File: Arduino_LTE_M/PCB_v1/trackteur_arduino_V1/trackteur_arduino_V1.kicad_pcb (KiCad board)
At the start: 2 copper layers, 94.7 x 56.3 mm, 24 parts, among them J1 rPi_HDR, J2 DC/DC, J3 BATT_CAR, J4 MicroSD_Breakout, Q1 2N3904, U1 LD1117S33TR_SOT223

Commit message: update PCB
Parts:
- removed H6, H7: MountingHole_2.7mm_M2.5, MountingHole:MountingHole_2.7mm_M2.5
- added G***: LOGO, footprint_project:logo_trackteur, B.Cu at (208.0, 83.7)
- added H2: MountingHole, MountingHole:MountingHole_2.7mm_M2.5, F.Cu at (134.1, 65.9)
- added H3: MountingHole, MountingHole:MountingHole_2.7mm_M2.5, F.Cu at (134.1, 72.9)
- added J5: Conn_02x02_Counter_Clockwise, Connector_PinHeader_2.54mm:PinHeader_2x02_P2.54mm_Vertical, F.Cu at (243.2, 50.0)
- added J6: Conn_01x06, Connector_PinHeader_2.54mm:PinHeader_1x06_P2.54mm_Vertical, F.Cu at (218.9, 69.8)
- added TP1: +5V, Connector_PinHeader_2.54mm:PinHeader_1x01_P2.54mm_Vertical, F.Cu at (167.0, 90.5)
- added TP2: GND, Connector_PinHeader_2.54mm:PinHeader_1x01_P2.54mm_Vertical, F.Cu at (176.1, 90.6)
- added TP3: +3.3V, Connector_PinHeader_2.54mm:PinHeader_1x01_P2.54mm_Vertical, F.Cu at (180.8, 74.8)
- H1: value MountingHole_2.7mm_M2.5 -> MountingHole
- moved Q1 34.0 mm to (167.3, 77.9), turned to -90 degrees
- moved R1 33.8 mm to (171.9, 84.0), turned to 90 degrees
- moved R2 30.6 mm to (162.3, 79.0)
- moved R4 30.0 mm to (186.8, 52.2), turned to -90 degrees
- moved H1 27.5 mm to (134.1, 59.0)
- moved D4 24.0 mm to (191.1, 62.5), turned to 90 degrees
- moved R3 14.1 mm to (201.6, 71.1), turned to 180 degrees
- moved C1 10.1 mm to (186.3, 93.1)
- moved D2 9.83 mm to (234.1, 74.3)
- moved D3 2.65 mm to (214.5, 71.0)
- moved D1 2.44 mm to (236.3, 93.9)
- moved C2 2.16 mm to (180.3, 84.6), turned to 90 degrees
- moved J3 0.45 mm to (243.8, 86.8)
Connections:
- A1 pad 10: unconnected-(A1-D7-Pad10) -> D7
- A1 pad 13: unconnected-(A1-D10-Pad13) -> D10
- A1 pad 19: unconnected-(A1-A0-Pad19) -> A0
- A1 pad 20: unconnected-(A1-A1-Pad20) -> A1
- A1 pad 21: unconnected-(A1-A2-Pad21) -> A2
- A1 pad 22: unconnected-(A1-A3-Pad22) -> A3
- A1 pad 8: unconnected-(A1-D5-Pad8) -> D5
- A1 pad 9: unconnected-(A1-D6-Pad9) -> D9
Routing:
- net GND: track 0.00 -> 228.5 mm
- net +5V: track 0.00 -> 171.4 mm
- net SCK: track 0.00 -> 70.3 mm, vias 0 -> 1
- net DI: track 0.00 -> 68.8 mm, vias 0 -> 1
- net TXD: track 0.00 -> 68.5 mm
- net DO: track 0.00 -> 68.0 mm, vias 0 -> 1
- net RXD: track 0.00 -> 66.2 mm
- net /CS: track 0.00 -> 60.9 mm
- net CD: track 0.00 -> 55.3 mm, vias 0 -> 1
- net TXD_5V: track 0.00 -> 52.0 mm
- net +3.3V: track 0.00 -> 44.5 mm
- net Net-(D2-A1): track 0.00 -> 25.6 mm
- net CTL: track 0.00 -> 20.0 mm
- net CTL_5V: track 0.00 -> 19.5 mm
- net Net-(D1-A): track 0.00 -> 14.8 mm
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
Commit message: Fichiers de fabrication
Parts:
- added G***: LOGO, footprint_project:logo_trackteur, F.Cu at (172.3, 48.4)
- J3: footprint Connector_Wire:SolderWire-0.75sqmm_1x02_P7mm_D1.25mm_OD3.5mm -> Connector_Wire:SolderWire-2.5sqmm_1x02_P7.2mm_D2.4mm_OD3.6mm
- moved H2 114.0 mm to (244.9, 92.8)
- moved H3 31.2 mm to (158.1, 92.8)
- moved H1 28.0 mm to (158.1, 44.6)
- moved G*** 7.78 mm to (200.5, 81.5)
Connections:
- J5 pad 1: A3 -> A2
- J5 pad 2: A2 -> A3
- J5 pad 3: A1 -> A0
- J5 pad 4: A0 -> A1
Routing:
- net GND: track 228.5 -> 271.4 mm
- net +5V: track 171.4 -> 208.0 mm
- net A3: track 0.00 -> 29.4 mm
- net A1: track 0.00 -> 24.8 mm
- net A2: track 0.00 -> 23.4 mm
- net A0: track 0.00 -> 18.1 mm
- net D5: track 0.00 -> 8.07 mm
- net D9: track 0.00 -> 7.12 mm
- net D7: track 0.00 -> 7.12 mm
- net D10: track 0.00 -> 4.00 mm
- net CTL: track 20.0 -> 19.5 mm
- added copper zone on B.Cu, net GND
- added copper zone on F.Cu, net GND
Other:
- board size 94.7 x 56.3 mm -> 95.4 x 56.8 mm
- board text added: "+5V"
- board text added: "/CS"
- board text added: "A0"
- board text added: "A1"
- board text added: "A2"
- board text added: "A3"
- board text added: "CD"
- board text added: "D10"
- board text added: "D5"
- board text added: "D7"
- board text added: "D9"
- board text added: "DI"
- board text added: "DO"
- board text added: "GND"
- board text added: "M2.5"
- board text added: "SCK"
- board text added: "v2025.04.01"

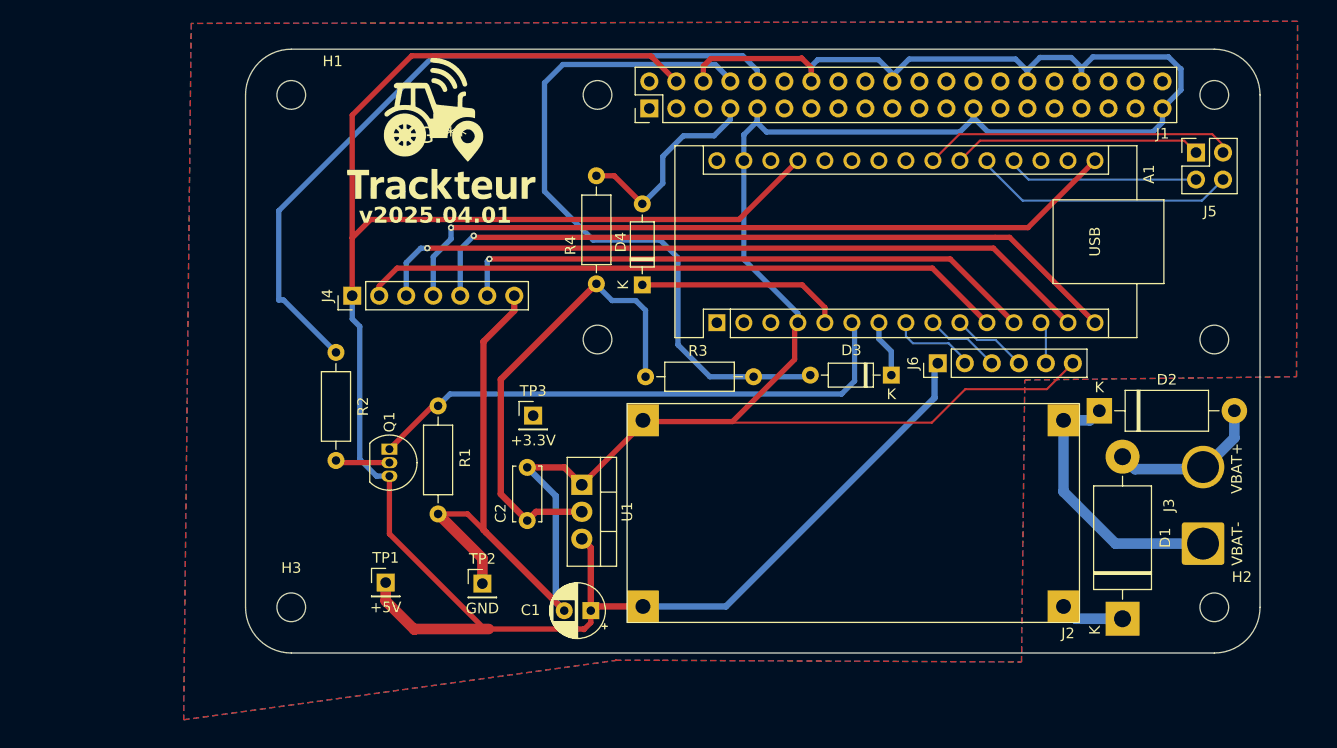
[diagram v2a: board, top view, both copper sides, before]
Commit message: LTE send dummy gps working and new pcb
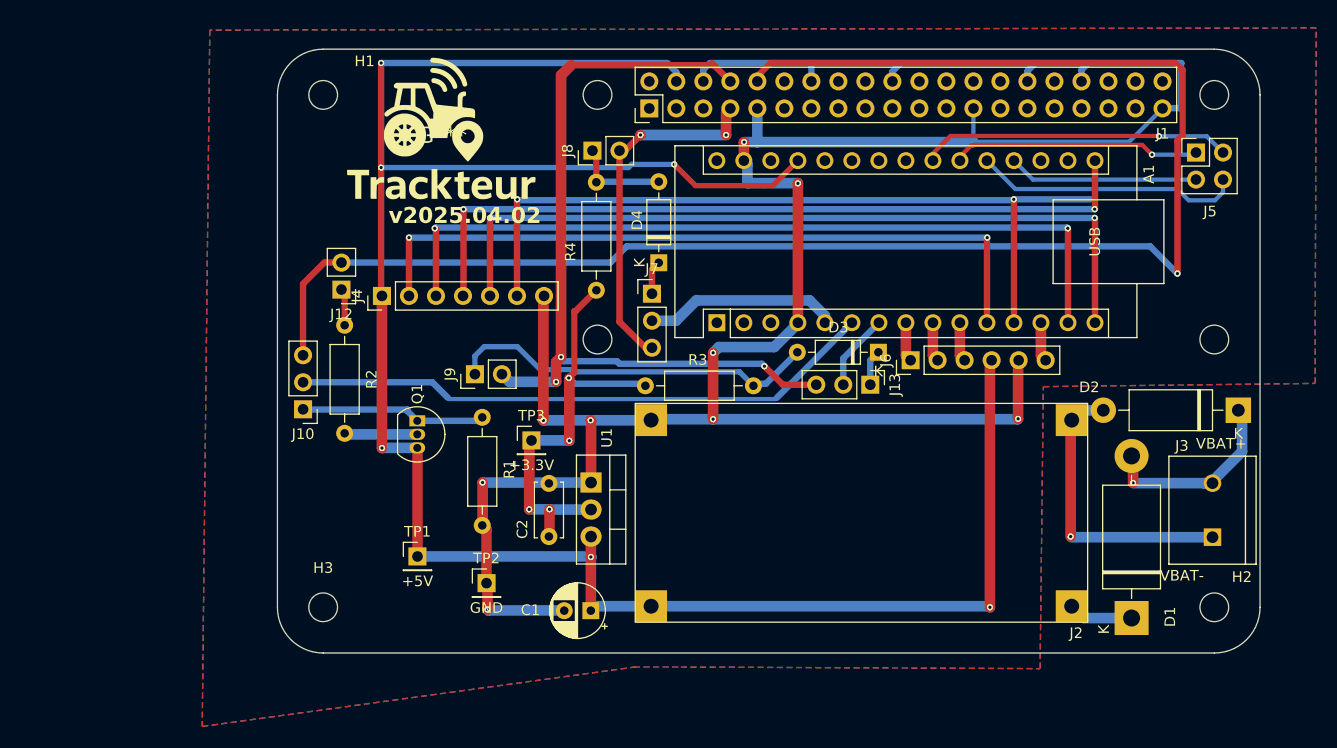
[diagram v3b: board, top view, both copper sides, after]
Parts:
- added J10: Conn_01x03, Connector_PinHeader_2.54mm:PinHeader_1x03_P2.54mm_Vertical, F.Cu at (159.2, 74.2)
- added J12: Conn_01x02, Connector_PinHeader_2.54mm:PinHeader_1x02_P2.54mm_Vertical, F.Cu at (162.8, 62.9)
- added J13: Conn_01x03, Connector_PinHeader_2.54mm:PinHeader_1x03_P2.54mm_Vertical, F.Cu at (212.6, 71.9)
- added J7: Conn_01x03, Connector_PinHeader_2.54mm:PinHeader_1x03_P2.54mm_Vertical, F.Cu at (192.0, 63.3)
- added J8: Conn_01x02, Connector_PinHeader_2.54mm:PinHeader_1x02_P2.54mm_Vertical, F.Cu at (186.4, 49.9)
- added J9: Conn_01x02, Connector_PinHeader_2.54mm:PinHeader_1x02_P2.54mm_Vertical, F.Cu at (175.4, 70.9)
- J3: footprint Connector_Wire:SolderWire-2.5sqmm_1x02_P7.2mm_D2.4mm_OD3.6mm -> footprint_project:TE_282837-2
- moved D2 13.1 mm to (247.2, 74.3), turned to 180 degrees
- moved R1 4.29 mm to (176.1, 85.1)
- moved TP1 3.87 mm to (170.0, 88.0)
- moved Q1 3.73 mm to (169.9, 75.3)
- moved J3 3.27 mm to (244.7, 83.7)
- moved H1 3.00 mm to (161.1, 44.6)
- moved H3 3.00 mm to (161.1, 92.8)
- moved J4 2.80 mm to (166.6, 63.5)
- moved R2 2.68 mm to (163.1, 76.4)
- moved D4 2.60 mm to (192.7, 60.4)
- moved J6 2.57 mm to (216.3, 69.6)
- moved C2 2.54 mm to (182.3, 86.2)
- moved D3 2.47 mm to (213.3, 68.8)
- moved TP3 2.34 mm to (180.7, 77.1)
- moved U1 0.89 mm to (186.3, 81.1)
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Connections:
- net Net-(D1-K) renamed /VBAT+2
- D1 pad 2: Net-(D1-A) -> /VBAT+
- D2 pad 1: Net-(D2-A1) -> /VBAT+
- D2 pad 2: Net-(D1-A) -> /VBAT-
- D3 pad 1: RXD_5V -> Net-(D3-K)
- D3 pad 2: RXD -> Net-(D3-A)
- D4 pad 1: CTL_5V -> Net-(D4-K)
- D4 pad 2: CTL -> Net-(D4-A)
- J2 pad 3: Net-(D2-A1) -> /VBAT-
- J3 pad 1: Net-(D2-A1) -> /VBAT-
- J3 pad 2: Net-(D1-A) -> /VBAT+
- J6 pad 1: +5V -> D5
- J6 pad 2: D5 -> D9
- J6 pad 3: D9 -> D7
- J6 pad 4: D7 -> +5V
- J6 pad 5: D10 -> GND
- J6 pad 6: GND -> D10
- Q1 pad 1: TXD_5V -> Net-(J10-Pin_1)
- R1 pad 2: TXD_5V -> Net-(J10-Pin_1)
- R2 pad 2: TXD -> Net-(J12-Pin_1)
- R3 pad 1: RXD -> Net-(D3-A)
- R4 pad 1: CTL -> Net-(D4-A)
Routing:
- net TXD: track 68.5 -> 152.1 mm, vias 0 -> 1
- net Net-(D3-A): track 0.00 -> 35.2 mm
- net GND: track 271.4 -> 242.1 mm, vias 0 -> 9
- net /VBAT-: track 0.00 -> 28.2 mm, vias 0 -> 1
- net Net-(D2-A1): track 25.6 -> 0.00 mm
- net CD: track 55.3 -> 74.7 mm, vias 1 -> 2
- net /VBAT+: track 0.00 -> 18.7 mm, vias 0 -> 1
- net Net-(J10-Pin_1): track 0.00 -> 17.5 mm
- net Net-(D1-A): track 14.8 -> 0.00 mm
- net CTL: track 19.5 -> 33.5 mm, vias 0 -> 2
- net RXD: track 66.2 -> 76.8 mm, vias 0 -> 3
- net Net-(D4-A): track 0.00 -> 9.01 mm
- net /CS: track 60.9 -> 67.9 mm, vias 0 -> 2
- net DO: track 68.0 -> 74.0 mm, vias 1 -> 2
- net DI: track 68.8 -> 74.9 mm, vias 1 -> 2
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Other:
- board size 95.4 x 56.8 mm -> 92.4 x 56.8 mm
- board text added: "v2025.04.02"
- board text removed: "v2025.04.01"

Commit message: update PCB gerbers
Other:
- board text added: "v2025.04.03"
- board text removed: "v2025.04.02"
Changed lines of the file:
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@@
     (effects (font (size 1.5 1.5) (thickness 0.3) bold) (justify left bottom mirror))
   )
-  (gr_text "v2025.04.02" (at 208.9404 90.2716) (layer "B.SilkS")
+  (gr_text "v2025.04.03" (at 208.9404 90.2716) (layer "B.SilkS")
     (effects (font (size 1.5 1.5) (thickness 0.3) bold) (justify left bottom mirror))
   )
@@
     (effects (font (size 1 1) (thickness 0.1)) (justify left bottom))
   )
-  (gr_text "v2025.04.02" (at 167.25 56.8412) (layer "F.SilkS")
+  (gr_text "v2025.04.03" (at 167.25 56.8412) (layer "F.SilkS")
     (effects (font (size 1.5 1.5) (thickness 0.3) bold) (justify left bottom))
   )
@@
     (connect_pads (clearance 0.5))
     (min_thickness 0.25) (filled_areas_thickness no)
-    (fill yes (mode hatch) (thermal_gap 0.5) (thermal_bridge_width 0.5)
-      (hatch_thickness 1) (hatch_gap 1.5) (hatch_orientation 0)
-      (hatch_border_algorithm hatch_thickness) (hatch_min_hole_area 0.3))
+    (fill yes (thermal_gap 0.5) (thermal_bridge_width 0.5))
     (polygon
       (pts
